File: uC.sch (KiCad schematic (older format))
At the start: 17 parts

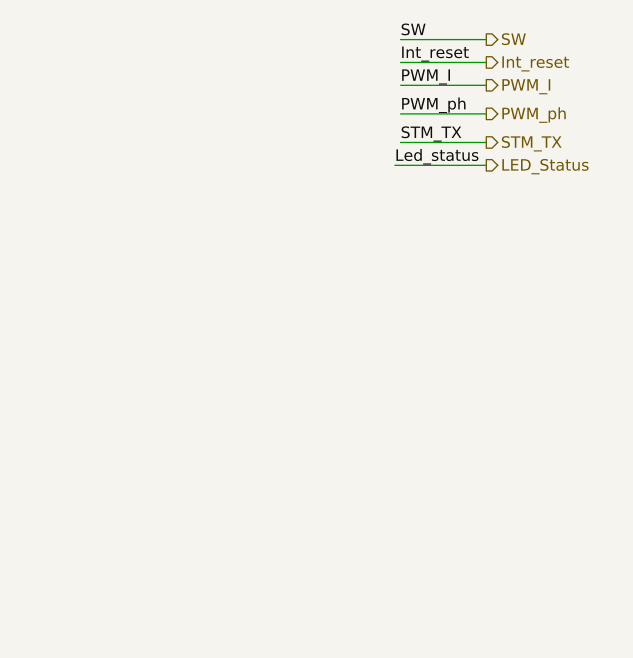
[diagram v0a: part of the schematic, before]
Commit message: Added laser diode, power stage, connecting block in progress
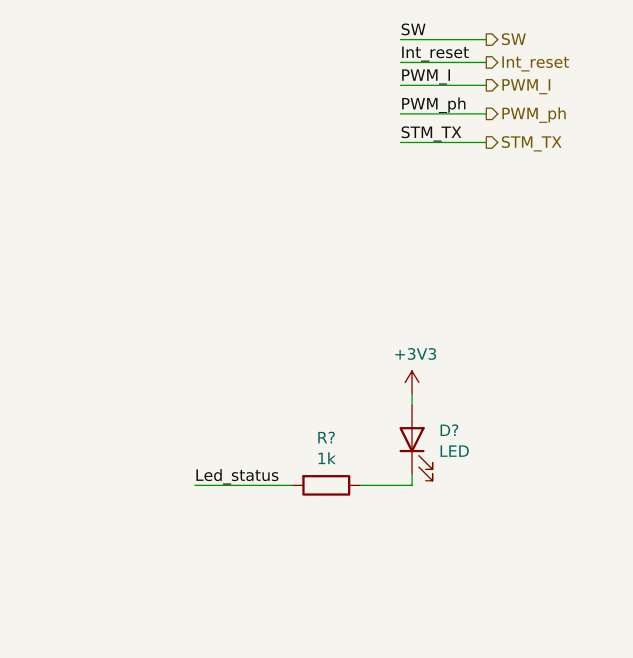
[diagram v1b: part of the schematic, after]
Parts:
- added D?: LED, symbol Device:LED
- added R?: 1k, symbol Device:R
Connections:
- net +3V3: now also D?.2 (A)
- net LED_Status renamed Led_status
- net Led_status: now also R?.2
- new net: D?.1 (K), R?.1
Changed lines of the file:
@@
 $Descr A4 11693 8268
 encoding utf-8
-Sheet 4 12
+Sheet 4 11
 Title ""
 Date ""
@@
 Text Label 10375 1000 0    50   ~ 0
 PWM_ph
-Text Label 10350 1225 0    50   ~ 0
-Led_status
 $Comp
 L power:GND #PWR?
@@
 Wire Wire Line
 	10375 1125 10750 1125
-Wire Wire Line
-	10350 1225 10750 1225
 Text HLabel 10750 1125 2    50   Output ~ 0
 STM_TX
-Text HLabel 10750 1225 2    50   Output ~ 0
-LED_Status
+Text Label 9475 2625 0    50   ~ 0
+Led_status
+$Comp
+L Device:LED D?
+U 1 1 61A4BB8B
+P 10425 2425
+F 0 "D?" V 10464 2307 50  0000 R CNN
+F 1 "LED" V 10373 2307 50  0000 R CNN
+F 2 "" H 10425 2425 50  0001 C CNN
+F 3 "~" H 10425 2425 50  0001 C CNN
+	1    10425 2425
+	0    -1   -1   0
+$EndComp
+$Comp
+L Device:R R?
+U 1 1 61A51FB7
+P 10050 2625
+F 0 "R?" V 9843 2625 50  0000 C CNN
+F 1 "1k" V 9934 2625 50  0000 C CNN
+F 2 "" V 9980 2625 50  0001 C CNN
+F 3 "~" H 10050 2625 50  0001 C CNN
+	1    10050 2625
+	0    1    1    0
+$EndComp
+Wire Wire Line
+	9475 2625 9900 2625
+Wire Wire Line
+	10200 2625 10425 2625
+Wire Wire Line
+	10425 2625 10425 2575
+$Comp
+L power:+3V3 #PWR?
+U 1 1 61A62195
+P 10425 2225
+F 0 "#PWR?" H 10425 2075 50  0001 C CNN
+F 1 "+3V3" H 10440 2398 50  0000 C CNN
+F 2 "" H 10425 2225 50  0001 C CNN
+F 3 "" H 10425 2225 50  0001 C CNN
+	1    10425 2225
+	1    0    0    -1
+$EndComp
+Wire Wire Line
+	10425 2225 10425 2275
 $EndSCHEMATC

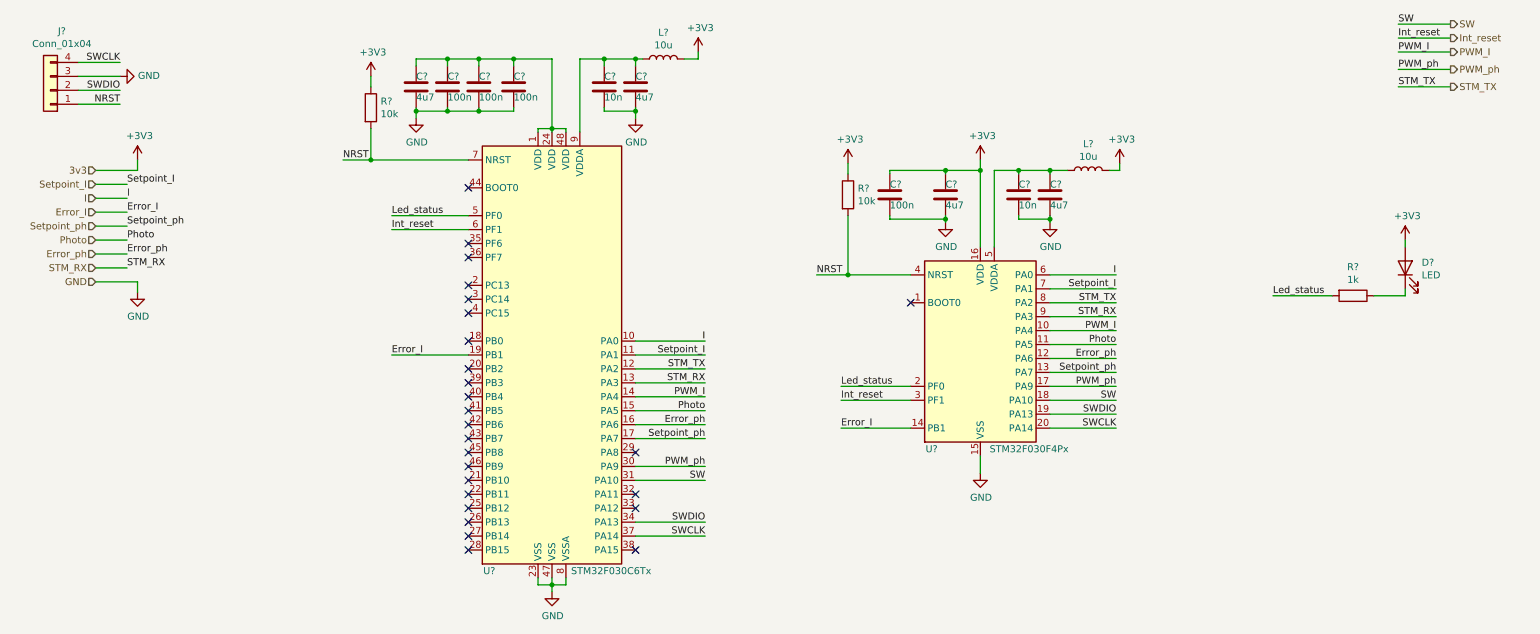
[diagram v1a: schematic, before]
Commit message: Removed uC setpoint measurements
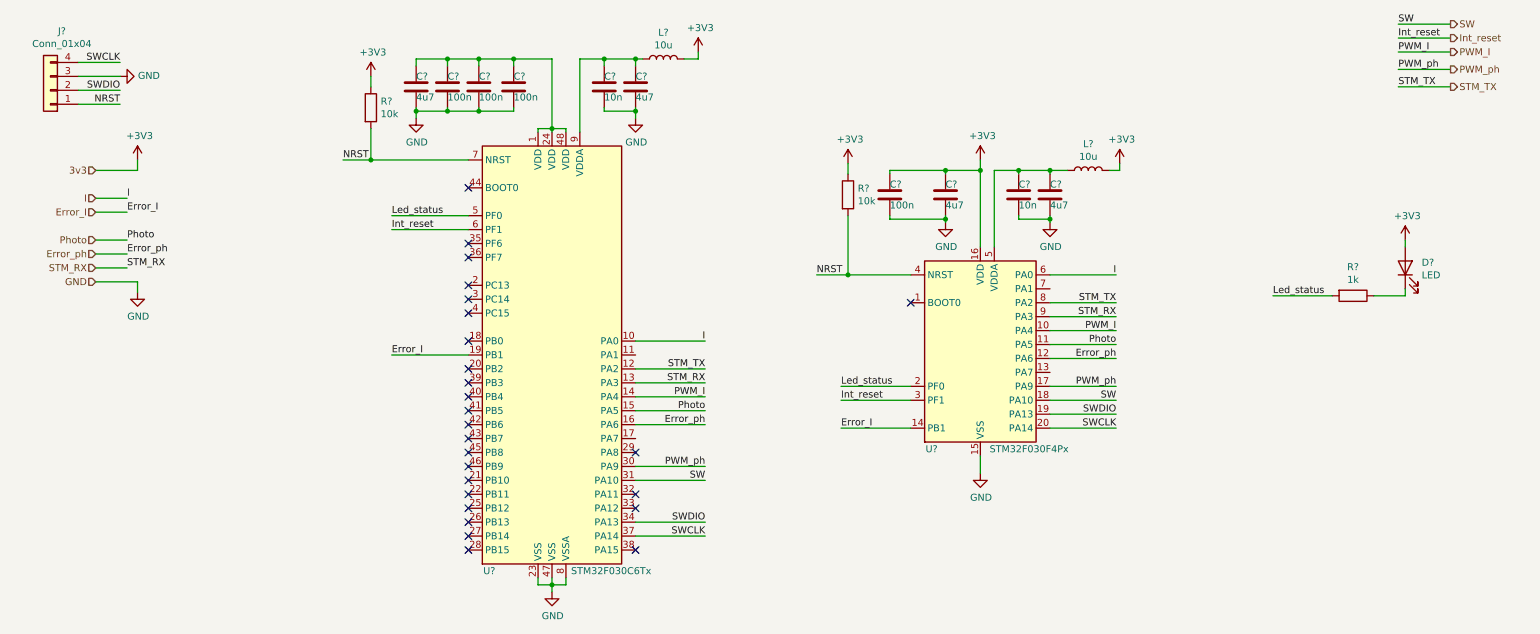
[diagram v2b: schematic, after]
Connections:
- net Setpoint_I: no longer names the net of U?.11 (PA1)
- net Setpoint_I: no longer U?.7 (PA1)
- net Setpoint_ph: no longer names the net of U?.17 (PA7)
- net Setpoint_ph: no longer U?.13 (PA7)
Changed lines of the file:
@@
 Text Label 8350 2475 2    50   ~ 0
 I
-Text Label 8350 2575 2    50   ~ 0
-Setpoint_I
 Text Label 8350 3075 2    50   ~ 0
 Error_ph
-Text Label 8350 3175 2    50   ~ 0
-Setpoint_ph
 Text Label 8350 2975 2    50   ~ 0
 Photo
@@
 	7875 3275 8350 3275
 Wire Wire Line
-	7875 3175 8350 3175
-Wire Wire Line
 	7875 3075 8350 3075
 Wire Wire Line
@@
 	7875 2675 8350 2675
 Wire Wire Line
-	7875 2575 8350 2575
-Wire Wire Line
 	7875 2475 8350 2475
 NoConn ~ 6875 2675
-Text Label 5400 3650 2    50   ~ 0
-Setpoint_ph
-Wire Wire Line
-	5400 3650 4900 3650
 Wire Wire Line
 	4900 4250 5400 4250
@@
 Wire Wire Line
 	4900 2950 5400 2950
-Text Label 5400 3050 2    50   ~ 0
-Setpoint_I
 Text Label 3150 3050 0    50   ~ 0
 Error_I
@@
 Wire Wire Line
 	4900 3150 5400 3150
-Wire Wire Line
-	4900 3050 5400 3050
 Text Label 5400 3350 2    50   ~ 0
 PWM_I
@@
 Text Label 10375 675  0    50   ~ 0
 SW
-Text Label 1250 1825 0    50   ~ 0
-Setpoint_I
 Text Label 1250 2025 0    50   ~ 0
 Error_I
@@
 Text Label 1250 2325 0    50   ~ 0
 Error_ph
-Text Label 1250 2125 0    50   ~ 0
-Setpoint_ph
 Text Label 10375 775  0    50   ~ 0
 Int_reset
@@
 Text HLabel 1025 1725 0    50   Input ~ 0
 3v3
-Text HLabel 1025 1825 0    50   Input ~ 0
-Setpoint_I
 Text HLabel 1025 1925 0    50   Input ~ 0
 I
 Text HLabel 1025 2025 0    50   Input ~ 0
 Error_I
-Text HLabel 1025 2125 0    50   Input ~ 0
-Setpoint_ph
 Text HLabel 1025 2225 0    50   Input ~ 0
 Photo
@@
 	1325 1725 1325 1650
 Wire Wire Line
-	1025 1825 1250 1825
-Wire Wire Line
 	1025 1925 1250 1925
 Wire Wire Line
 	1025 2025 1250 2025
 Wire Wire Line
-	1025 2125 1250 2125
-Wire Wire Line
 	1025 2225 1250 2225
